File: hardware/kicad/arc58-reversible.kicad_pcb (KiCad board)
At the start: 2 copper layers, 172.8 x 149.2 mm, 91 parts, among them J1 MJ-4PP-9_Reversible, J2 SSD1306 OLED 128x32, SW1 SW_PUSH_LED, SW10 SW_PUSH_LED, SW11 SW_PUSH_LED, SW12 SW_PUSH_LED, SW13 SW_PUSH_LED, SW14 SW_PUSH_LED, SW15 SW_PUSH_LED, SW16 SW_PUSH_LED, SW17 SW_PUSH_LED, SW18 SW_PUSH_LED, SW19 SW_PUSH_LED, SW2 SW_PUSH_LED, SW20 SW_PUSH_LED, SW21 SW_PUSH_LED, SW22 SW_PUSH_LED, SW23 SW_PUSH_LED, SW24 SW_PUSH_LED, SW25 EC11_Clickable_H20mm_T18, SW26 SW_PUSH_LED, SW27 SW_PUSH_LED, SW28 SW_PUSH_LED, SW29 SW_PUSH_LED, SW3 SW_PUSH_LED, SW4 SW_PUSH_LED, SW5 SW_PUSH_LED, SW6 SW_PUSH_LED, SW7 SW_PUSH_LED, SW8 SW_PUSH_LED, SW9 SW_PUSH_LED, U1 KEEBD Helios RP2040, U2 74AHCT1G125

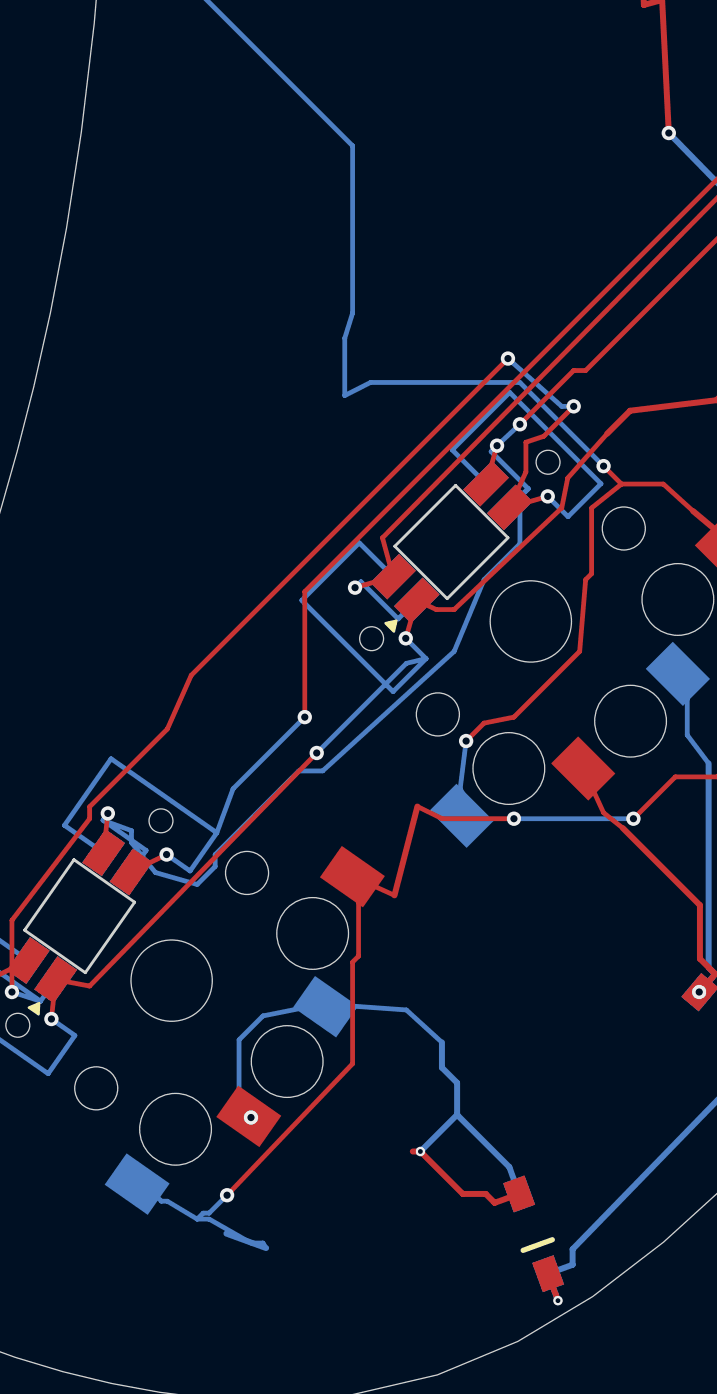
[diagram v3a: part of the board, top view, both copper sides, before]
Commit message: Simplify Rev Beta copper routing
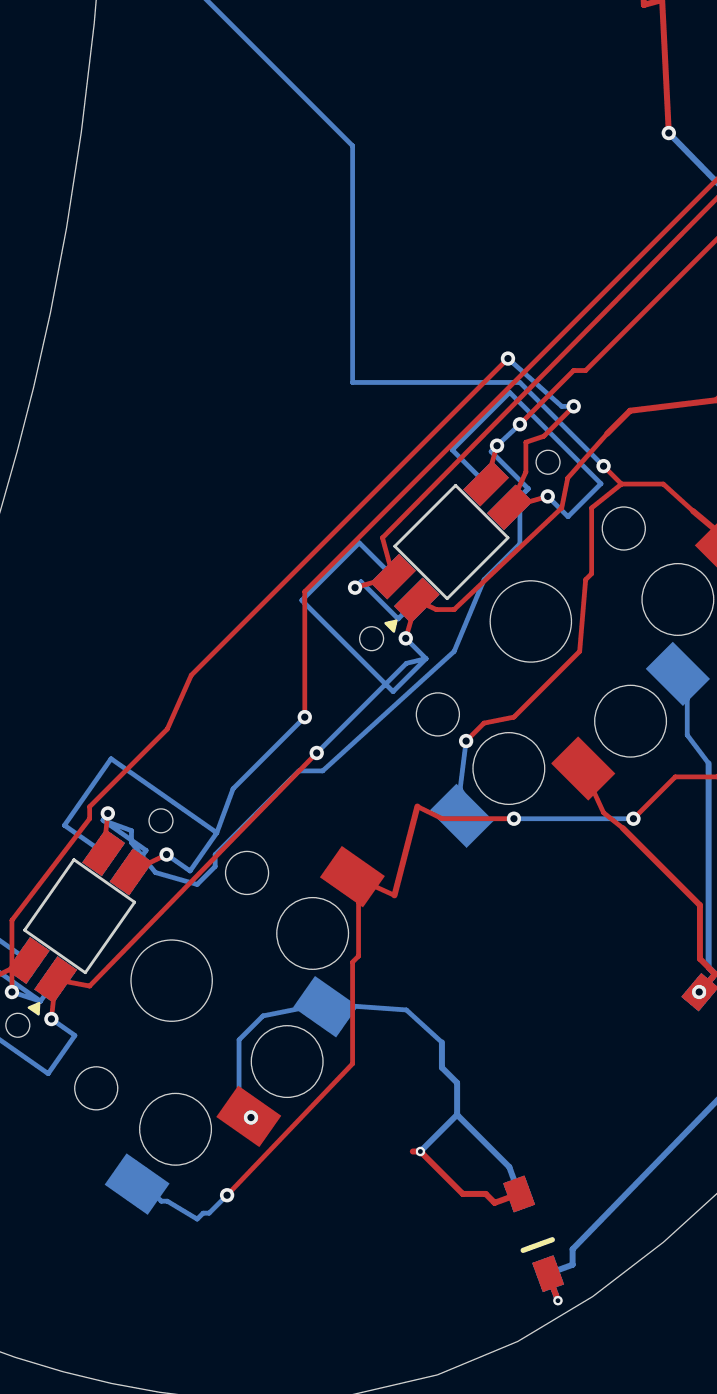
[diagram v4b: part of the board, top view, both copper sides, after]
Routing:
- net COL4: track 317.9 -> 312.8 mm
- net COL3: track 329.2 -> 328.1 mm
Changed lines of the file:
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@@
 		(net "SPLIT_DATA")
 	)
-	(segment
-		(start 126.689 99.473)
-		(end 127.46186 98.699989)
-		(width 0.25)
-		(locked yes)
-		(layer "F.Cu")
-		(net "ROW3")
-	)
-	(segment
-		(start 157.533 47.464)
-		(end 160.457 47.464)
-		(width 0.25)
-		(locked yes)
-		(layer "F.Cu")
-		(net "COL3")
-	)
-	(segment
-		(start 156.49862 99.194106)
-		(end 156.499 99.8748)
-		(width 0.25)
-		(locked yes)
-		(layer "B.Cu")
-		(net "Net-(SW21-Pad2)")
-	)
-	(segment
-		(start 133.04201 81.93253)
-		(end 133.042 77.4153)
-		(width 0.25)
-		(locked yes)
-		(layer "B.Cu")
-		(net "Net-(SW14-Pad2)")
-	)
 	(via
 		(at 94.75 80)
@@
 	)
 	(segment
+		(start 126.689 99.473)
+		(end 127.46186 98.699989)
+		(width 0.25)
+		(locked yes)
+		(layer "F.Cu")
+		(net "ROW3")
+	)
+	(segment
 		(start 169.016 100.642)
 		(end 168.907 100.532)
@@
 	)
 	(segment
-		(start 81.75 170.5)
-		(end 82.25 170.5)
-		(width 0.2)
-		(layer "B.Cu")
-		(net "COL4")
-	)
-	(segment
 		(start 122.25 67)
 		(end 122.25 66.75)
@@
 	)
 	(segment
-		(start 82.382834 170.709855)
-		(end 80.720728 170.104978)
-		(width 0.25)
-		(layer "B.Cu")
-		(net "COL4")
-	)
-	(segment
 		(start 110.25 67.25)
 		(end 109.75 66.75)
@@
 	)
 	(segment
-		(start 82.25 170.5)
-		(end 82.382834 170.709855)
-		(width 0.2)
-		(layer "B.Cu")
-		(net "COL4")
-	)
-	(segment
 		(start 131.7 89.3)
 		(end 131.7 88.196)
@@
 	)
 	(segment
-		(start 80 169.5)
-		(end 81.75 170.5)
-		(width 0.2)
-		(layer "B.Cu")
-		(net "COL4")
-	)
-	(segment
 		(start 124.75 67.5)
 		(end 124.25 67.5)
@@
 	)
 	(segment
-		(start 79.5 169.5)
-		(end 80 169.5)
-		(width 0.2)
-		(layer "B.Cu")
-		(net "COL4")
-	)
-	(segment
 		(start 127.588 66.7058)
 		(end 127.5 66.75)
@@
 	)
 	(segment
+		(start 157.533 47.464)
+		(end 160.457 47.464)
+		(width 0.25)
+		(locked yes)
+		(layer "F.Cu")
+		(net "COL3")
+	)
+	(segment
 		(start 117 61.6)
 		(end 117.4 61.6)
@@
 	)
 	(segment
-		(start 85.672577 135.04773)
-		(end 86.75 134.5)
-		(width 0.2)
-		(layer "B.Cu")
-		(net "COL3")
-	)
-	(segment
 		(start 80 81.4)
 		(end 79 81.4)
@@
 	)
 	(segment
-		(start 85.672577 132.64773)
-		(end 85.672577 135.04773)
-		(width 0.2)
-		(layer "B.Cu")
-		(net "COL3")
-	)
-	(segment
 		(start 108.2 64)
 		(end 108.6 64)
@@
 	)
 	(segment
-		(start 86.75 134.5)
-		(end 93 134.5)
-		(width 0.2)
-		(layer "B.Cu")
-		(net "COL3")
-	)
-	(segment
 		(start 150.85 86.8)
 		(end 150.8 86.75)
@@
 	)
 	(segment
+		(start 86 134.5)
+		(end 93 134.5)
+		(width 0.2)
+		(layer "B.Cu")
+		(net "COL3")
+	)
+	(segment
 		(start 128 60.8)
 		(end 128.4 60.8)
@@
 	)
 	(segment
-		(start 86 124.6)
-		(end 86 131.6)
-		(width 0.2)
-		(layer "B.Cu")
-		(net "COL3")
-	)
-	(segment
 		(start 150.85 48.7)
 		(end 153.015 46.5353)
@@
 	)
 	(segment
-		(start 156.886 48.1107)
-		(end 157.533 47.464)
-		(width 0.25)
+		(start 86 124.6)
+		(end 86 134.5)
+		(width 0.2)
 		(layer "B.Cu")
 		(net "COL3")
 	)
 	(segment
-		(start 86 131.6)
-		(end 85.672577 132.64773)
-		(width 0.2)
+		(start 156.886 48.1107)
+		(end 157.533 47.464)
+		(width 0.25)
 		(layer "B.Cu")
 		(net "COL3")
@@
 	)
 	(segment
+		(start 156.49862 99.194106)
+		(end 156.499 99.8748)
+		(width 0.25)
+		(locked yes)
+		(layer "B.Cu")
+		(net "Net-(SW21-Pad2)")
+	)
+	(segment
 		(start 147.6591 121.77)
 		(end 146.165 121.77)
@@
 		(net "Net-(SW14-Pad2)")
 	)
+	(segment
+		(start 133.04201 81.93253)
+		(end 133.042 77.4153)
+		(width 0.25)
+		(locked yes)
+		(layer "B.Cu")
+		(net "Net-(SW14-Pad2)")
+	)

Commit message: Update Arc 58 firmware for Elite-Pi
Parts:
- moved D26 7.98 mm to (87.0, 165.5), turned to -125 degrees
- moved D29 6.21 mm to (133.6, 140.4), turned to 10 degrees
- moved D27 6.02 mm to (101.6, 152.6), turned to -135 degrees
- moved D28 1.65 mm to (115.9, 141.1)
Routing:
- net Net-(D26-Pad2): track 28.3 -> 16.8 mm
- net Net-(D29-Pad2): track 12.8 -> 20.3 mm, vias 1 -> 2
- net ROW4: track 183.5 -> 189.4 mm
- net Net-(D27-Pad2): track 25.9 -> 30.7 mm, vias 1 -> 2
- net Net-(D28-Pad2): track 12.7 -> 16.8 mm
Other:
- board text added: "REV GAMMA • REVERSIBLE LEFT / RIGHT"
- board text removed: "REV BETA • REVERSIBLE LEFT / RIGHT"

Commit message: fix keyboard layout
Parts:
- moved D29 3.95 mm to (130.8, 137.6)
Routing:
- net COL2: track 370.8 -> 364.9 mm
- net Net-(D29-Pad2): track 20.3 -> 25.5 mm
- net ROW4: track 189.4 -> 187.5 mm
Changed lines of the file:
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@@
 	(footprint "Reversible_Diode_SOD123"
 		(layer "F.Cu")
-		(at 133.592898 140.429712 10)
+		(at 130.83912 137.60264 10)
 		(descr "One diode, mountable on either board side; pad geometry follows the Sofle Choc reversible diode")
 		(property "Reference" "D29"
@@
 	)
 	(segment
-		(start 131.844864 140.737937)
-		(end 130.860056 140.911585)
+		(start 129.091086 137.910865)
+		(end 128.204759 138.067148)
 		(width 0.25)
 		(layer "F.Cu")
@@
 	(segment
 		(start 118.734421 139.46306)
-		(end 130.860056 140.911585)
+		(end 129.091086 137.910865)
 		(width 0.25)
 		(layer "F.Cu")
@@
 	)
 	(via
-		(at 130.860056 140.911585)
+		(at 128.204759 138.067148)
 		(size 0.4)
 		(drill 0.2)
@@
 	)
 	(segment
-		(start 131.844864 140.737937)
-		(end 130.860056 140.911585)
+		(start 129.091086 137.910865)
+		(end 128.204759 138.067148)
 		(width 0.25)
 		(layer "B.Cu")
@@
 	)
 	(segment
-		(start 107.205188 118.068293)
+		(start 100.905512 117)
 		(end 99.837219 118.068293)
 		(width 0.25)
@@
 	)
 	(segment
-		(start 111.842 112.946)
-		(end 107.205188 118.068293)
+		(start 111.842 117)
+		(end 100.905512 117)
 		(width 0.25)
 		(layer "F.Cu")
@@
 	)
 	(segment
-		(start 111.842 117)
-		(end 111.842 112.946)
-		(width 0.25)
-		(layer "F.Cu")
-		(net "COL2")
-	)
-	(segment
 		(start 185.6 50.6835)
 		(end 185.6 51.2)
@@
 	)
 	(segment
-		(start 135.340932 140.121487)
+		(start 132.587154 137.294415)
 		(end 135.427756 140.613891)
 		(width 0.25)
@@
 		(net "Net-(D29-Pad2)")
 	)
+	(segment
+		(start 132.587154 137.294415)
+		(end 133.473481 137.138132)
+		(width 0.25)
+		(layer "F.Cu")
+		(net "Net-(D29-Pad2)")
+	)
 	(via
 		(at 134.912862 132.472589)
@@
 	)
 	(via
-		(at 135.427756 140.613891)
+		(at 133.473481 137.138132)
 		(size 0.4)
 		(drill 0.2)
@@
 	)
 	(segment
-		(start 135.340932 140.121487)
-		(end 135.427756 140.613891)
+		(start 132.587154 137.294415)
+		(end 133.473481 137.138132)
 		(width 0.25)
 		(layer "B.Cu")
